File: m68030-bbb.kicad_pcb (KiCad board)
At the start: 4 copper layers, 177.8 x 127 mm, 12 parts, among them U1 MC68030, U10 M29F160F, U11 M29F160F, U12 XC95108TQ100, U2 R68561, U3 68230, U4 CY62167GN-45ZXI, U5 CY62167GN-45ZXI, U6 CY62167GN-45ZXI, U7 CY62167GN-45ZXI, U8 M29F160F, U9 M29F160F

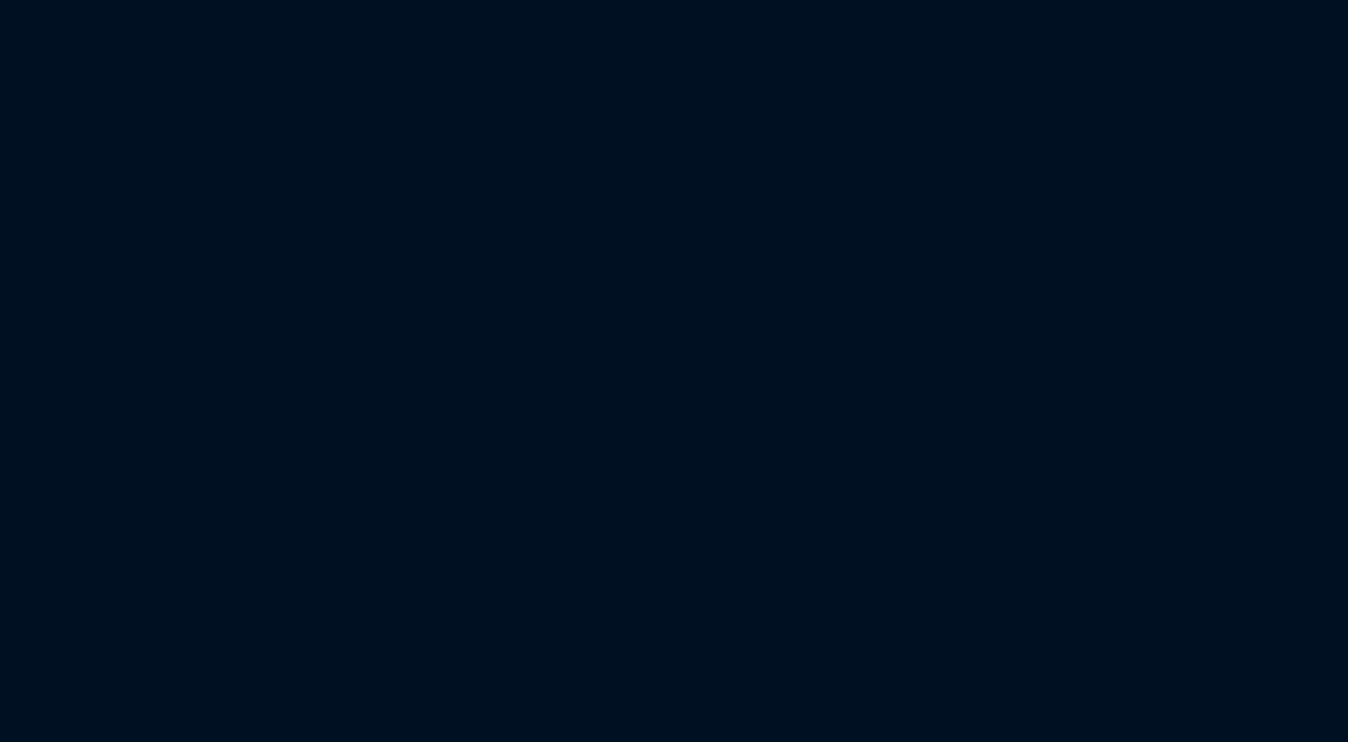
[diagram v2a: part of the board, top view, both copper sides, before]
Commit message: More CPLD changes, counter and comparitor for DTACK generation testing in sim.
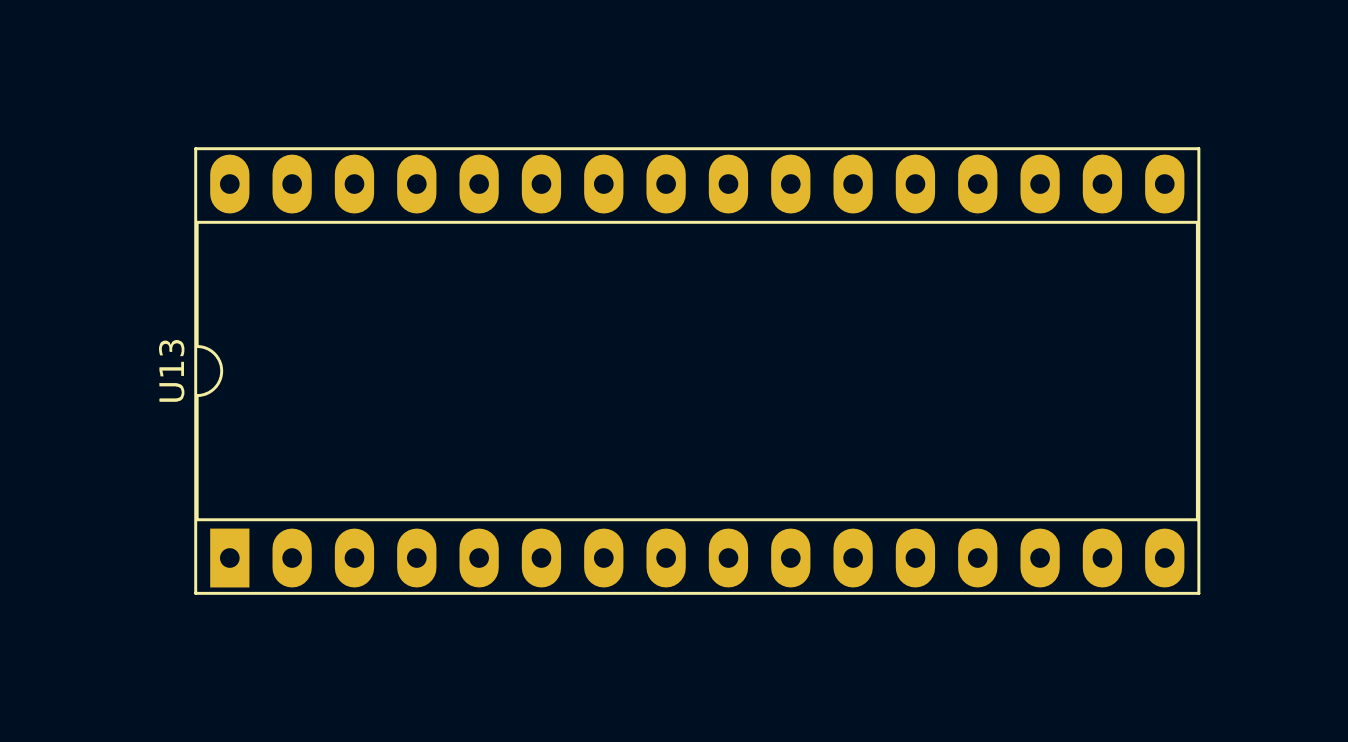
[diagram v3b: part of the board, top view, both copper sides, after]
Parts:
- added U13: SST39SF010, Package_DIP:DIP-32_W15.24mm_Socket_LongPads, F.Cu at (183.6, 89.9)
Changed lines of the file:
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@@
   (net 387 "unconnected-(U12-Pad96)")
   (net 388 "unconnected-(U12-Pad97)")
+  (net 389 "unconnected-(U13-Pad1)")
+  (net 390 "unconnected-(U13-Pad2)")
+  (net 391 "unconnected-(U13-Pad3)")
+  (net 392 "unconnected-(U13-Pad4)")
+  (net 393 "unconnected-(U13-Pad5)")
+  (net 394 "unconnected-(U13-Pad6)")
+  (net 395 "unconnected-(U13-Pad7)")
+  (net 396 "unconnected-(U13-Pad8)")
+  (net 397 "unconnected-(U13-Pad9)")
+  (net 398 "unconnected-(U13-Pad10)")
+  (net 399 "unconnected-(U13-Pad11)")
+  (net 400 "unconnected-(U13-Pad12)")
+  (net 401 "unconnected-(U13-Pad13)")
+  (net 402 "unconnected-(U13-Pad14)")
+  (net 403 "unconnected-(U13-Pad15)")
+  (net 404 "unconnected-(U13-Pad17)")
+  (net 405 "unconnected-(U13-Pad18)")
+  (net 406 "unconnected-(U13-Pad19)")
+  (net 407 "unconnected-(U13-Pad20)")
+  (net 408 "unconnected-(U13-Pad21)")
+  (net 409 "unconnected-(U13-Pad22)")
+  (net 410 "unconnected-(U13-Pad23)")
+  (net 411 "unconnected-(U13-Pad24)")
+  (net 412 "unconnected-(U13-Pad25)")
+  (net 413 "unconnected-(U13-Pad26)")
+  (net 414 "unconnected-(U13-Pad27)")
+  (net 415 "unconnected-(U13-Pad28)")
+  (net 416 "unconnected-(U13-Pad29)")
+  (net 417 "unconnected-(U13-Pad30)")
+  (net 418 "unconnected-(U13-Pad31)")
+  (net 419 "VCC")
   (footprint "Package_DIP:DIP-48_W15.24mm_Socket_LongPads" (layer "F.Cu")
     (at 99.06 129.545 90)
@@
       (offset (xyz 0 0 0))
       (scale (xyz 1 1 1))
+      (rotate (xyz 0 0 0))
+    )
+  )
+  (footprint "Package_DIP:DIP-32_W15.24mm_Socket_LongPads" (layer "F.Cu")
+    (at 183.642 89.916 90)
+    (descr "32-lead though-hole mounted DIP package, row spacing 15.24 mm (600 mils), Socket, LongPads")
+    (tags "THT DIP DIL PDIP 2.54mm 15.24mm 600mil Socket LongPads")
+    (property "Sheetfile" "m68030-bbb.kicad_sch")
+    (property "Sheetname" "")
+    (attr through_hole)
+    (fp_text reference "U13" (at 7.62 -2.33 90) (layer "F.SilkS")
+      (effects (font (size 1 1) (thickness 0.15)))
+    )
+    (fp_text value "SST39SF010" (at 7.62 40.43 90) (layer "F.Fab")
+      (effects (font (size 1 1) (thickness 0.15)))
+    )
+    (fp_text user "${REFERENCE}" (at 7.62 19.05 90) (layer "F.Fab")
+      (effects (font (size 1 1) (thickness 0.15)))
+    )
+    (fp_line (start 16.68 -1.39) (end -1.44 -1.39) (layer "F.SilkS") (width 0.12))
+    (fp_line (start 16.68 39.49) (end 16.68 -1.39) (layer "F.SilkS") (width 0.12))
+    (fp_line (start -1.44 -1.39) (end -1.44 39.49) (layer "F.SilkS") (width 0.12))
+    (fp_line (start 13.68 -1.33) (end 8.62 -1.33) (layer "F.SilkS") (width 0.12))
+    (fp_line (start 1.56 -1.33) (end 1.56 39.43) (layer "F.SilkS") (width 0.12))
+    (fp_line (start 6.62 -1.33) (end 1.56 -1.33) (layer "F.SilkS") (width 0.12))
+    (fp_line (start 13.68 39.43) (end 13.68 -1.33) (layer "F.SilkS") (width 0.12))
+    (fp_line (start 1.56 39.43) (end 13.68 39.43) (layer "F.SilkS") (width 0.12))
+    (fp_line (start -1.44 39.49) (end 16.68 39.49) (layer "F.SilkS") (width 0.12))
+    (fp_arc (start 8.62 -1.33) (mid 7.62 -0.33) (end 6.62 -1.33) (layer "F.SilkS") (width 0.12))
+    (fp_line (start -1.55 -1.6) (end -1.55 39.7) (layer "F.CrtYd") (width 0.05))
+    (fp_line (start -1.55 39.7) (end 16.8 39.7) (layer "F.CrtYd") (width 0.05))
+    (fp_line (start 16.8 -1.6) (end -1.55 -1.6) (layer "F.CrtYd") (width 0.05))
+    (fp_line (start 16.8 39.7) (end 16.8 -1.6) (layer "F.CrtYd") (width 0.05))
+    (fp_line (start 16.51 -1.33) (end -1.27 -1.33) (layer "F.Fab") (width 0.1))
+    (fp_line (start -1.27 39.43) (end 16.51 39.43) (layer "F.Fab") (width 0.1))
+    (fp_line (start 0.255 39.37) (end 0.255 -0.27) (layer "F.Fab") (width 0.1))
+    (fp_line (start 0.255 -0.27) (end 1.255 -1.27) (layer "F.Fab") (width 0.1))
+    (fp_line (start 14.985 -1.27) (end 14.985 39.37) (layer "F.Fab") (width 0.1))
+    (fp_line (start -1.27 -1.33) (end -1.27 39.43) (layer "F.Fab") (width 0.1))
+    (fp_line (start 1.255 -1.27) (end 14.985 -1.27) (layer "F.Fab") (width 0.1))
+    (fp_line (start 14.985 39.37) (end 0.255 39.37) (layer "F.Fab") (width 0.1))
+    (fp_line (start 16.51 39.43) (end 16.51 -1.33) (layer "F.Fab") (width 0.1))
+    (pad "1" thru_hole rect (at 0 0 90) (size 2.4 1.6) (drill 0.8) (layers *.Cu *.Mask)
+      (net 389 "unconnected-(U13-Pad1)") (pinfunction "NC") (pintype "input"))
+    (pad "2" thru_hole oval (at 0 2.54 90) (size 2.4 1.6) (drill 0.8) (layers *.Cu *.Mask)
+      (net 390 "unconnected-(U13-Pad2)") (pinfunction "A16") (pintype "input"))
+    (pad "3" thru_hole oval (at 0 5.08 90) (size 2.4 1.6) (drill 0.8) (layers *.Cu *.Mask)
+      (net 391 "unconnected-(U13-Pad3)") (pinfunction "A15") (pintype "input"))
+    (pad "4" thru_hole oval (at 0 7.62 90) (size 2.4 1.6) (drill 0.8) (layers *.Cu *.Mask)
+      (net 392 "unconnected-(U13-Pad4)") (pinfunction "A12") (pintype "input"))
+    (pad "5" thru_hole oval (at 0 10.16 90) (size 2.4 1.6) (drill 0.8) (layers *.Cu *.Mask)
+      (net 393 "unconnected-(U13-Pad5)") (pinfunction "A7") (pintype "input"))
+    (pad "6" thru_hole oval (at 0 12.7 90) (size 2.4 1.6) (drill 0.8) (layers *.Cu *.Mask)
+      (net 394 "unconnected-(U13-Pad6)") (pinfunction "A6") (pintype "input"))
+    (pad "7" thru_hole oval (at 0 15.24 90) (size 2.4 1.6) (drill 0.8) (layers *.Cu *.Mask)
+      (net 395 "unconnected-(U13-Pad7)") (pinfunction "A5") (pintype "input"))
+    (pad "8" thru_hole oval (at 0 17.78 90) (size 2.4 1.6) (drill 0.8) (layers *.Cu *.Mask)
+      (net 396 "unconnected-(U13-Pad8)") (pinfunction "A4") (pintype "input"))
+    (pad "9" thru_hole oval (at 0 20.32 90) (size 2.4 1.6) (drill 0.8) (layers *.Cu *.Mask)
+      (net 397 "unconnected-(U13-Pad9)") (pinfunction "A3") (pintype "input"))
+    (pad "10" thru_hole oval (at 0 22.86 90) (size 2.4 1.6) (drill 0.8) (layers *.Cu *.Mask)
+      (net 398 "unconnected-(U13-Pad10)") (pinfunction "A2") (pintype "input"))
+    (pad "11" thru_hole oval (at 0 25.4 90) (size 2.4 1.6) (drill 0.8) (layers *.Cu *.Mask)
+      (net 399 "unconnected-(U13-Pad11)") (pinfunction "A1") (pintype "input"))
+    (pad "12" thru_hole oval (at 0 27.94 90) (size 2.4 1.6) (drill 0.8) (layers *.Cu *.Mask)
+      (net 400 "unconnected-(U13-Pad12)") (pinfunction "A0") (pintype "input"))
+    (pad "13" thru_hole oval (at 0 30.48 90) (size 2.4 1.6) (drill 0.8) (layers *.Cu *.Mask)
+      (net 401 "unconnected-(U13-Pad13)") (pinfunction "D0") (pintype "tri_state"))
+    (pad "14" thru_hole oval (at 0 33.02 90) (size 2.4 1.6) (drill 0.8) (layers *.Cu *.Mask)
+      (net 402 "unconnected-(U13-Pad14)") (pinfunction "D1") (pintype "tri_state"))
+    (pad "15" thru_hole oval (at 0 35.56 90) (size 2.4 1.6) (drill 0.8) (layers *.Cu *.Mask)
+      (net 403 "unconnected-(U13-Pad15)") (pinfunction "D2") (pintype "tri_state"))
+    (pad "16" thru_hole oval (at 0 38.1 90) (size 2.4 1.6) (drill 0.8) (layers *.Cu *.Mask)
+      (net 317 "GND") (pinfunction "GND") (pintype "power_in"))
+    (pad "17" thru_hole oval (at 15.24 38.1 90) (size 2.4 1.6) (drill 0.8) (layers *.Cu *.Mask)
+      (net 404 "unconnected-(U13-Pad17)") (pinfunction "D3") (pintype "tri_state"))
+    (pad "18" thru_hole oval (at 15.24 35.56 90) (size 2.4 1.6) (drill 0.8) (layers *.Cu *.Mask)
+      (net 405 "unconnected-(U13-Pad18)") (pinfunction "D4") (pintype "tri_state"))
+    (pad "19" thru_hole oval (at 15.24 33.02 90) (size 2.4 1.6) (drill 0.8) (layers *.Cu *.Mask)
+      (net 406 "unconnected-(U13-Pad19)") (pinfunction "D5") (pintype "tri_state"))
+    (pad "20" thru_hole oval (at 15.24 30.48 90) (size 2.4 1.6) (drill 0.8) (layers *.Cu *.Mask)
+      (net 407 "unconnected-(U13-Pad20)") (pinfunction "D6") (pintype "tri_state"))
+    (pad "21" thru_hole oval (at 15.24 27.94 90) (size 2.4 1.6) (drill 0.8) (layers *.Cu *.Mask)
+      (net 408 "unconnected-(U13-Pad21)") (pinfunction "D7") (pintype "tri_state"))
+    (pad "22" thru_hole oval (at 15.24 25.4 90) (size 2.4 1.6) (drill 0.8) (layers *.Cu *.Mask)
+      (net 409 "unconnected-(U13-Pad22)") (pinfunction "CE") (pintype "input"))
+    (pad "23" thru_hole oval (at 15.24 22.86 90) (size 2.4 1.6) (drill 0.8) (layers *.Cu *.Mask)
+      (net 410 "unconnected-(U13-Pad23)") (pinfunction "A10") (pintype "input"))
+    (pad "24" thru_hole oval (at 15.24 20.32 90) (size 2.4 1.6) (drill 0.8) (layers *.Cu *.Mask)
+      (net 411 "unconnected-(U13-Pad24)") (pinfunction "OE") (pintype "input"))
+    (pad "25" thru_hole oval (at 15.24 17.78 90) (size 2.4 1.6) (drill 0.8) (layers *.Cu *.Mask)
+      (net 412 "unconnected-(U13-Pad25)") (pinfunction "A11") (pintype "input"))
+    (pad "26" thru_hole oval (at 15.24 15.24 90) (size 2.4 1.6) (drill 0.8) (layers *.Cu *.Mask)
+      (net 413 "unconnected-(U13-Pad26)") (pinfunction "A9") (pintype "input"))
+    (pad "27" thru_hole oval (at 15.24 12.7 90) (size 2.4 1.6) (drill 0.8) (layers *.Cu *.Mask)
+      (net 414 "unconnected-(U13-Pad27)") (pinfunction "A8") (pintype "input"))
+    (pad "28" thru_hole oval (at 15.24 10.16 90) (size 2.4 1.6) (drill 0.8) (layers *.Cu *.Mask)
+      (net 415 "unconnected-(U13-Pad28)") (pinfunction "A13") (pintype "input"))
+    (pad "29" thru_hole oval (at 15.24 7.62 90) (size 2.4 1.6) (drill 0.8) (layers *.Cu *.Mask)
+      (net 416 "unconnected-(U13-Pad29)") (pinfunction "A14") (pintype "input"))
+    (pad "30" thru_hole oval (at 15.24 5.08 90) (size 2.4 1.6) (drill 0.8) (layers *.Cu *.Mask)
+      (net 417 "unconnected-(U13-Pad30)") (pinfunction "NC") (pintype "input"))
+    (pad "31" thru_hole oval (at 15.24 2.54 90) (size 2.4 1.6) (drill 0.8) (layers *.Cu *.Mask)
+      (net 418 "unconnected-(U13-Pad31)") (pinfunction "PGM") (pintype "input"))
+    (pad "32" thru_hole oval (at 15.24 0 90) (size 2.4 1.6) (drill 0.8) (layers *.Cu *.Mask)
+      (net 419 "VCC") (pinfunction "VCC") (pintype "power_in"))
+    (model "${KICAD6_3DMODEL_DIR}/Package_DIP.3dshapes/DIP-32_W15.24mm_Socket.wrl"
+      (offset (xyz 0 0 0))
+      (scale (xyz 1 1 1))

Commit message: Filled the CPLD... Not 100% sure this will run at 25MHz...  Maybe 20 or 16, design could probably use some optimization.
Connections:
- U10 pad 11: /~{WELL} -> /~{WEUM}
- U10 pad 26: /~{RDLL} -> /~{ROMCE}
- U10 pad 27: unconnected-(U10-Pad27) -> GND
- U10 pad 28: /~{ROMCE} -> /~{RDUM}
- U10 pad 46: unconnected-(U10-Pad46) -> GND
- U11 pad 11: /~{WELL} -> /~{WEUU}
- U11 pad 26: /~{RDLL} -> /~{ROMCE}
- U11 pad 27: unconnected-(U11-Pad27) -> GND
- U11 pad 28: /~{ROMCE} -> /~{RDUU}
- U11 pad 46: unconnected-(U11-Pad46) -> GND
- U12 pad 10: /FC1 -> /~{BERR}
- U12 pad 11: /FC2 -> unconnected-(U12-Pad11)
- U12 pad 46: unconnected-(U12-Pad46) -> /D24
- U12 pad 50: unconnected-(U12-Pad50) -> /D25
- U12 pad 52: unconnected-(U12-Pad52) -> /D26
- U12 pad 53: unconnected-(U12-Pad53) -> /D27
- U12 pad 54: unconnected-(U12-Pad54) -> /D28
- U12 pad 55: unconnected-(U12-Pad55) -> /D29
- U12 pad 56: unconnected-(U12-Pad56) -> /D30
- U12 pad 58: unconnected-(U12-Pad58) -> /D31
- U12 pad 59: unconnected-(U12-Pad59) -> /~{RAMCE}
- U12 pad 60: unconnected-(U12-Pad60) -> /~{ROMCE}
- U12 pad 61: unconnected-(U12-Pad61) -> /~{BOOTCE}
- U12 pad 63: unconnected-(U12-Pad63) -> /~{R561CE}
- U12 pad 64: unconnected-(U12-Pad64) -> /~{M230CE}
- U12 pad 9: /FC0 -> /~{HALT}
- U13 pad 10: unconnected-(U13-Pad10) -> /A2
- U13 pad 11: unconnected-(U13-Pad11) -> /A1
- U13 pad 12: unconnected-(U13-Pad12) -> /A0
- U13 pad 13: unconnected-(U13-Pad13) -> /D24
- U13 pad 14: unconnected-(U13-Pad14) -> /D25
- U13 pad 15: unconnected-(U13-Pad15) -> /D26
- U13 pad 17: unconnected-(U13-Pad17) -> /D27
- U13 pad 18: unconnected-(U13-Pad18) -> /D28
- U13 pad 19: unconnected-(U13-Pad19) -> /D29
- U13 pad 2: unconnected-(U13-Pad2) -> /A16
- U13 pad 20: unconnected-(U13-Pad20) -> /D30
- U13 pad 21: unconnected-(U13-Pad21) -> /D31
- U13 pad 22: unconnected-(U13-Pad22) -> /~{BOOTCE}
- U13 pad 23: unconnected-(U13-Pad23) -> /A10
- U13 pad 24: unconnected-(U13-Pad24) -> GND
- U13 pad 25: unconnected-(U13-Pad25) -> /A11
- U13 pad 26: unconnected-(U13-Pad26) -> /A9
- U13 pad 27: unconnected-(U13-Pad27) -> /A8
- U13 pad 28: unconnected-(U13-Pad28) -> /A13
- U13 pad 29: unconnected-(U13-Pad29) -> /A14
- U13 pad 3: unconnected-(U13-Pad3) -> /A15
- U13 pad 31: unconnected-(U13-Pad31) -> /R/~{W}
- U13 pad 32: VCC -> +5V
- U13 pad 4: unconnected-(U13-Pad4) -> /A12
- U13 pad 5: unconnected-(U13-Pad5) -> /A7
- U13 pad 6: unconnected-(U13-Pad6) -> /A6
- U13 pad 7: unconnected-(U13-Pad7) -> /A5
- U13 pad 8: unconnected-(U13-Pad8) -> /A4
- U13 pad 9: unconnected-(U13-Pad9) -> /A3
- U2 pad 11: unconnected-(U2-Pad11) -> GND
- U2 pad 16: unconnected-(U2-Pad16) -> /D20
- U2 pad 21: unconnected-(U2-Pad21) -> /D21
- U2 pad 28: unconnected-(U2-Pad28) -> /D22
- U2 pad 29: unconnected-(U2-Pad29) -> +5V
- U2 pad 32: unconnected-(U2-Pad32) -> /D31
- U2 pad 33: unconnected-(U2-Pad33) -> /D23
- U2 pad 34: unconnected-(U2-Pad34) -> /D30
- U2 pad 35: unconnected-(U2-Pad35) -> /D29
- U2 pad 36: unconnected-(U2-Pad36) -> /D28
- U2 pad 37: unconnected-(U2-Pad37) -> /D27
- U2 pad 38: unconnected-(U2-Pad38) -> /D26
- U2 pad 39: unconnected-(U2-Pad39) -> /D25
- U2 pad 4: unconnected-(U2-Pad4) -> /D18
- U2 pad 40: unconnected-(U2-Pad40) -> /D16
- U2 pad 41: unconnected-(U2-Pad41) -> /D24
- U2 pad 42: unconnected-(U2-Pad42) -> GND
- U2 pad 45: unconnected-(U2-Pad45) -> /D17
- U2 pad 8: unconnected-(U2-Pad8) -> /D19
- U3 pad 12: unconnected-(U3-Pad12) -> +5V
- U8 pad 26: /~{RDLL} -> /~{ROMCE}
- U8 pad 27: unconnected-(U8-Pad27) -> GND
- U8 pad 28: /~{ROMCE} -> /~{RDLL}
- U8 pad 46: unconnected-(U8-Pad46) -> GND
- U9 pad 11: /~{WELL} -> /~{WELM}
- U9 pad 26: /~{RDLL} -> /~{ROMCE}
- U9 pad 27: unconnected-(U9-Pad27) -> GND
- U9 pad 28: /~{ROMCE} -> /~{RDLM}
- U9 pad 46: unconnected-(U9-Pad46) -> GND
